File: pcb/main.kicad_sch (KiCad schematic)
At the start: 26 parts, among them J1 out+, J2 out-, J3 RP2040, J4 Conn_01x12_Socket, J5 Conn_01x12_Socket, SW1 SW_Push, U1 DRV2605LDGS

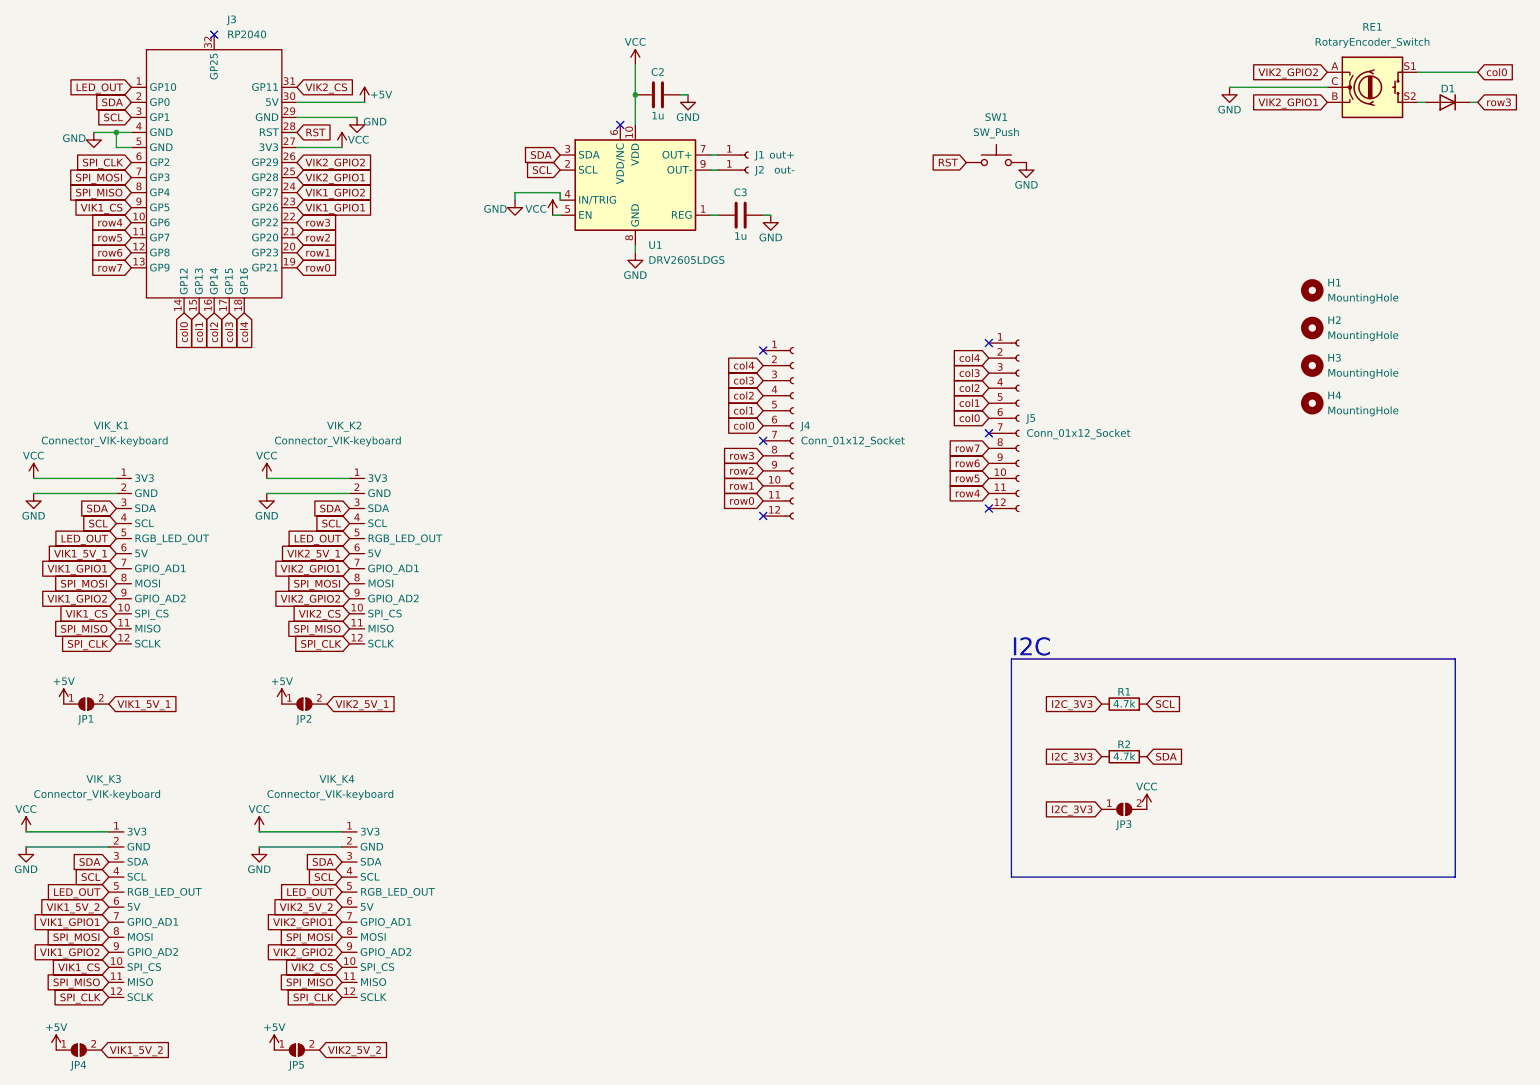
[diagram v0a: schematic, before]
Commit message: jumpers for VIK GPIO, small side updates
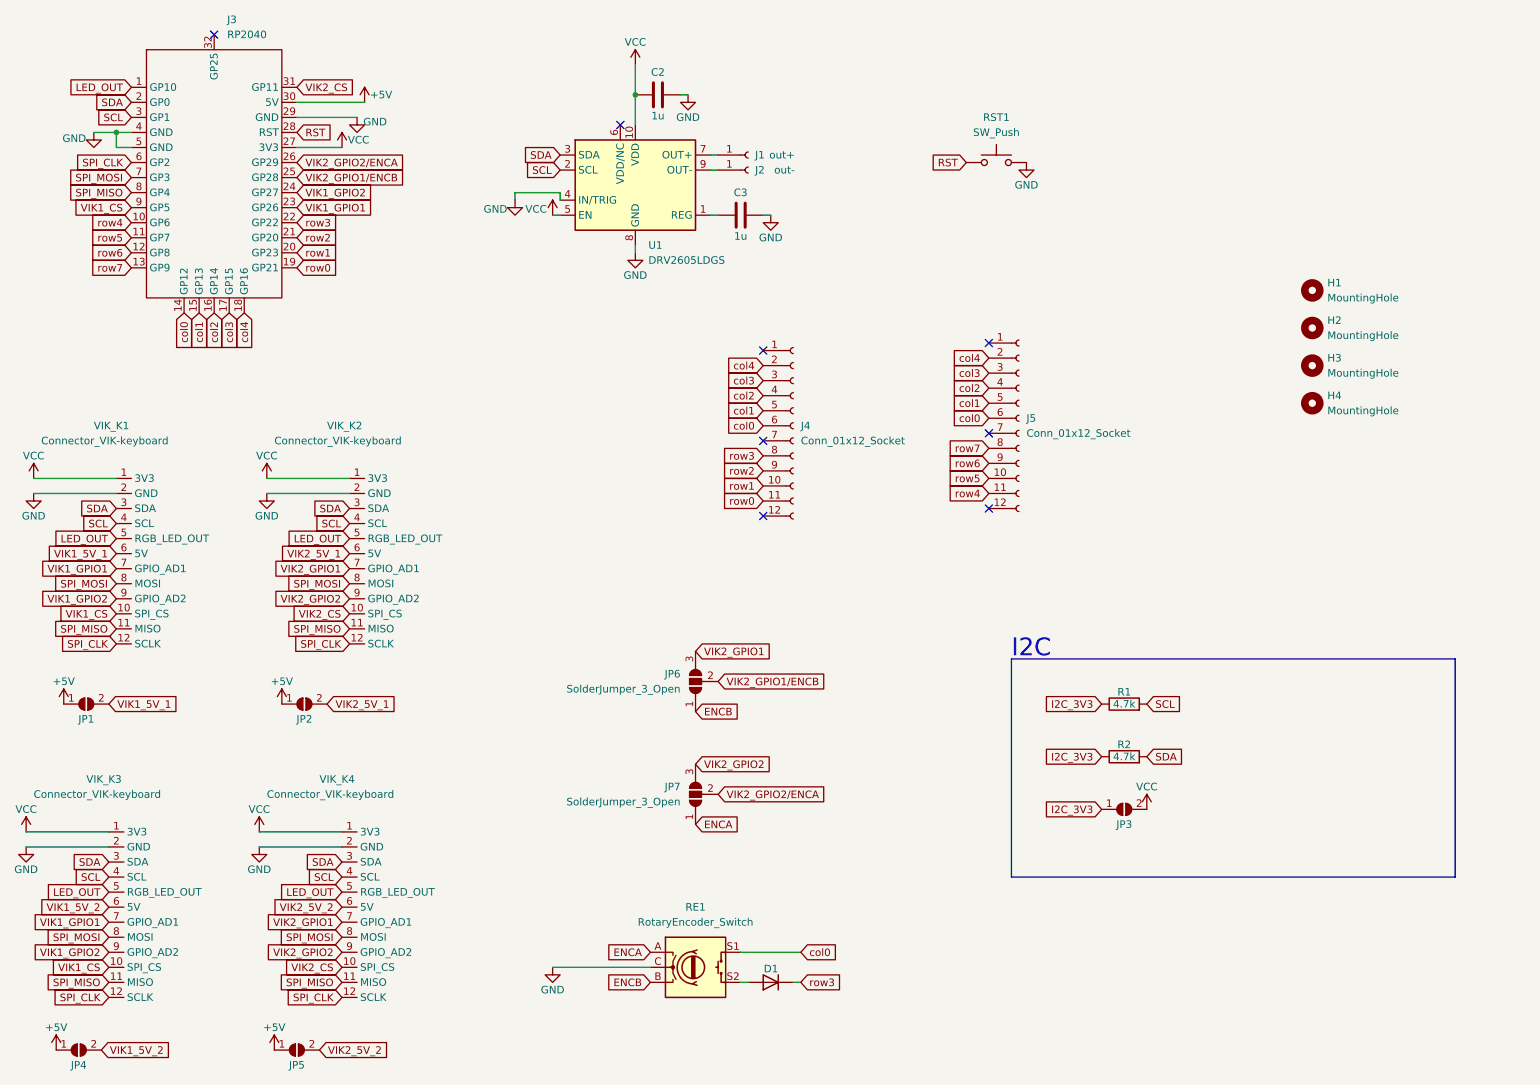
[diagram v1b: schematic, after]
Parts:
- added JP6, JP7: SolderJumper_3_Open, Jumper:SolderJumper-3_P1.3mm_Open_Pad1.0x1.5mm, symbol Jumper:SolderJumper_3_Open
- JP1, JP2, JP4, JP5: value SolderJumper_2_Open -> 5V
- JP3: value SolderJumper_2_Open -> VCC
- renumbered SW1 to RST1
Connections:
- net VIK2_GPIO1: now also JP6.3 (B); no longer J3.25 (GP28), RE1.B
- net VIK2_GPIO2: now also JP7.3 (B); no longer J3.26 (GP29), RE1.A
- new net ENCA: JP7.1 (A), RE1.A
- new net ENCB: JP6.1 (A), RE1.B
- new net VIK2_GPIO1/ENCB: J3.25 (GP28), JP6.2 (C)
- new net VIK2_GPIO2/ENCA: J3.26 (GP29), JP7.2 (C)
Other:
- moved on the sheet: D1, RE1
